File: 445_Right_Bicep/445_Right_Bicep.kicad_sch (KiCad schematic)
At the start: 7 parts, among them J1 69167-114HLF, J2 SM02B-SRSS-TB_LF__SN_, J3 87583-2010RPLF, U1 ESP32-S3-WROOM-1-N16R8, U2 LSM6DSMTR, U3 LP2950CZ-3.3_LFT3

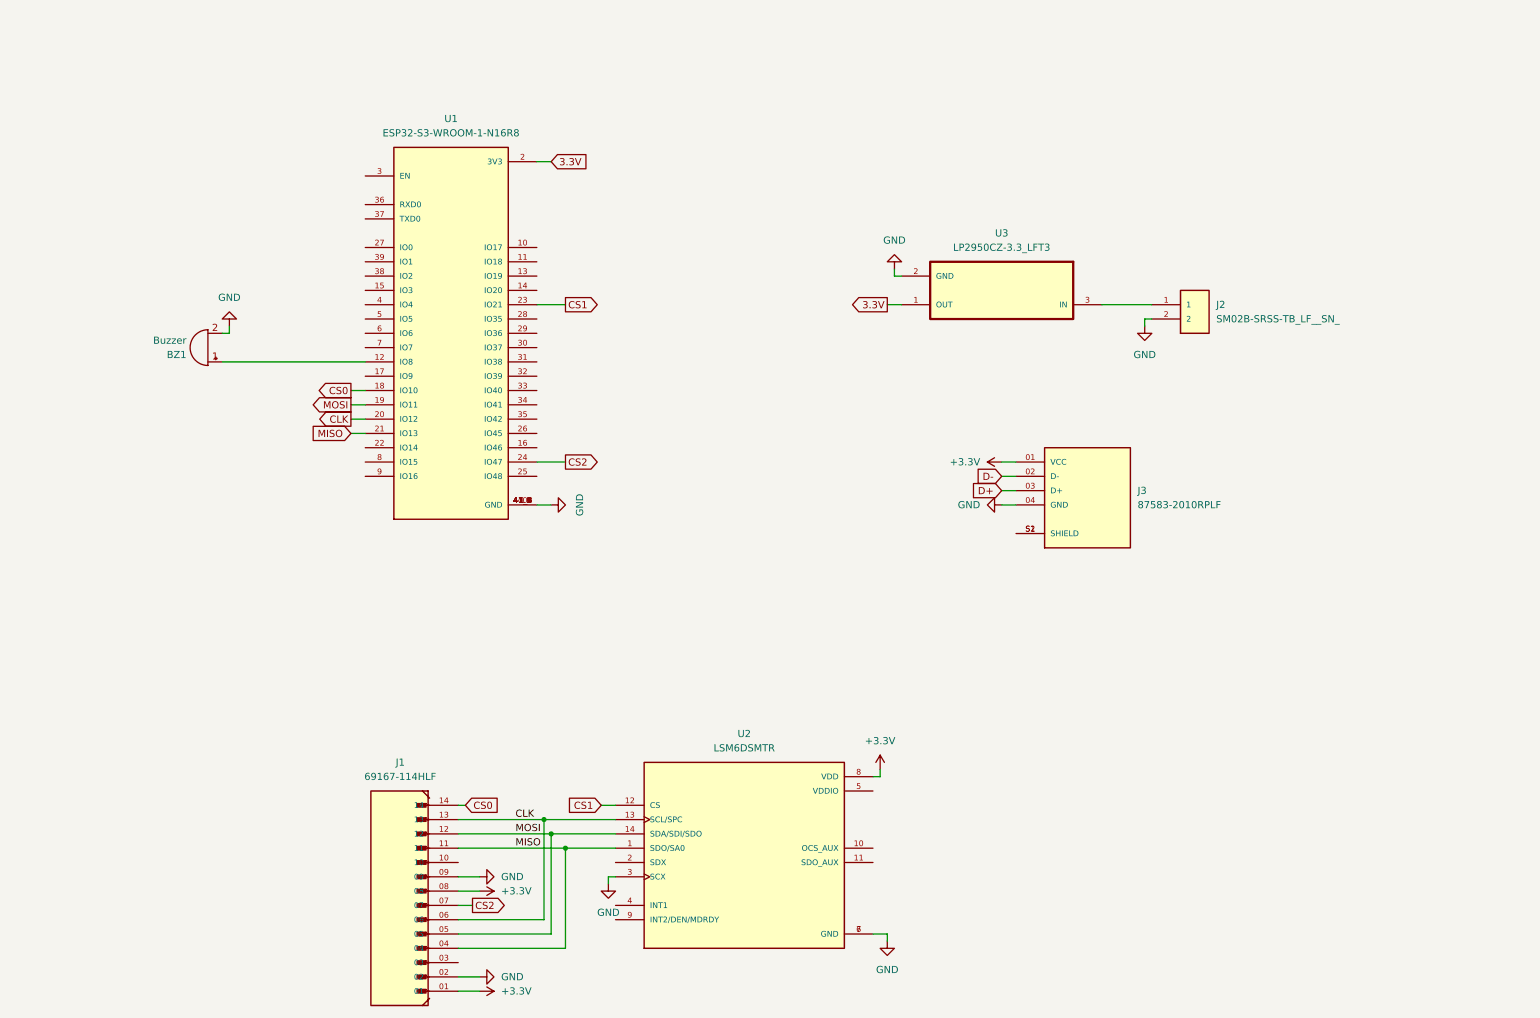
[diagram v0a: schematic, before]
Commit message: enable signal and analog switches
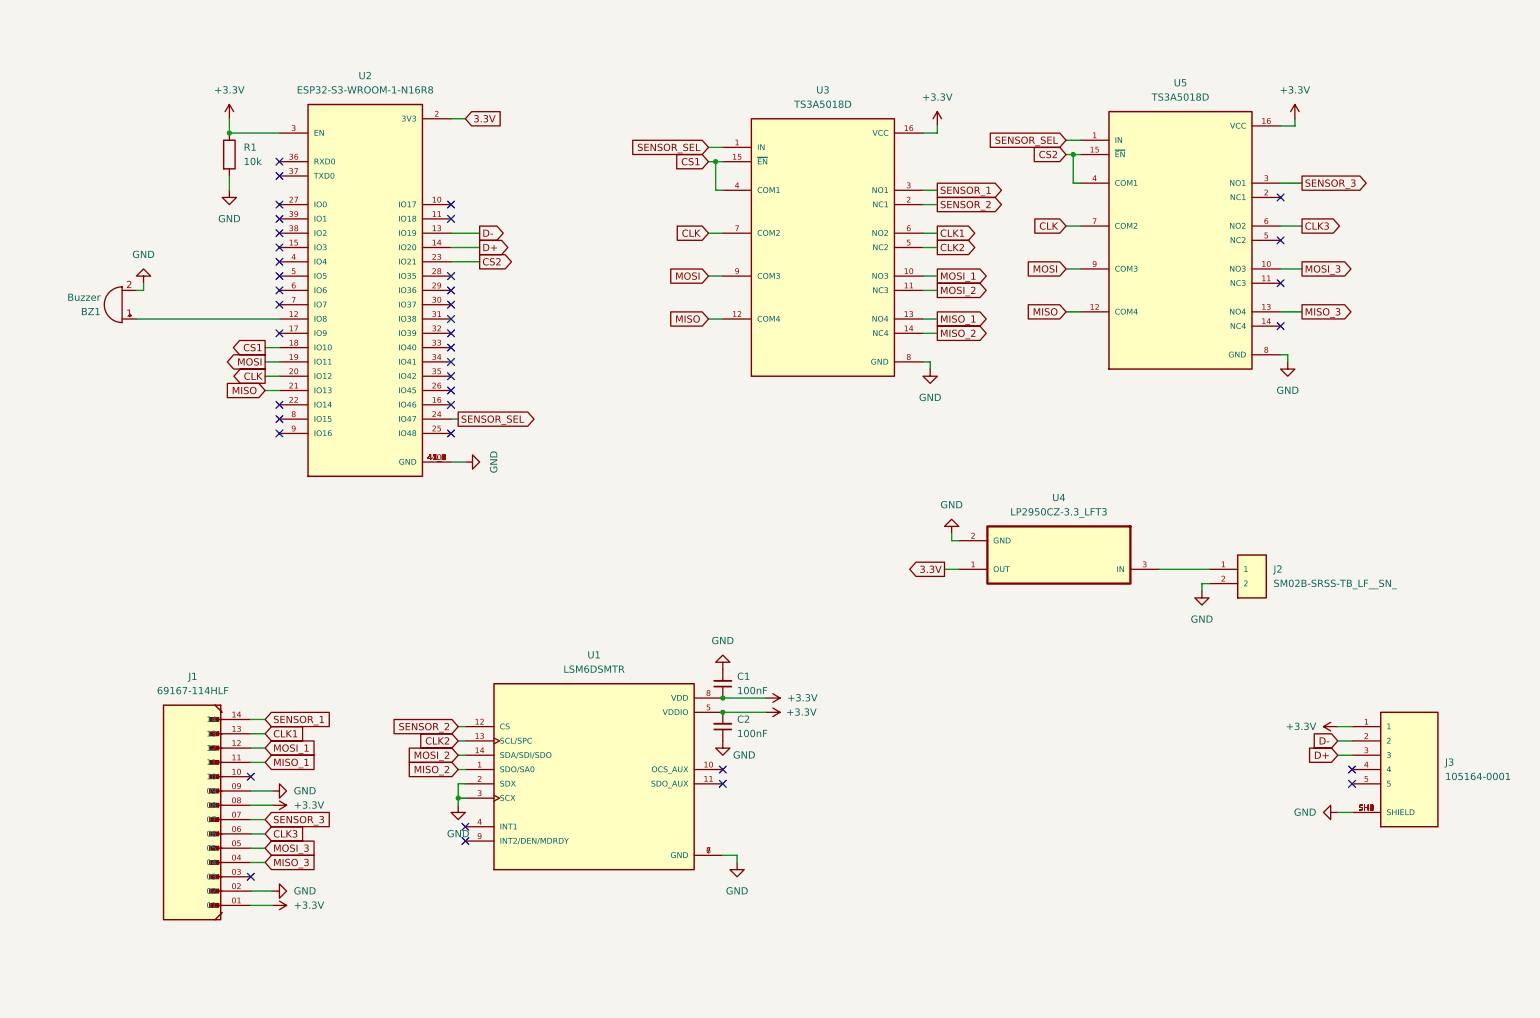
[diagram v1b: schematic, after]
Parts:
- removed J3: 87583-2010RPLF, 87583-2010RPLF:AMPHENOL_87583-2010RPLF, symbol 87583-2010RPLF:87583-2010RPLF
- removed U1: ESP32-S3-WROOM-1-N16R8, ESP32-S3-WROOM-1-N16R8:XCVR_ESP32-S3-WROOM-1-N16R8, symbol ESP32-S3-WROOM-1-N16R8:ESP32-S3-WROOM-1-N16R8
- removed U2: LSM6DSMTR, LSM6DSMTR (1):PQFN50P300X250X86-14N, symbol LSM6DSMTR:LSM6DSMTR
- removed U3: LP2950CZ-3.3_LFT3, LP2950CZ-3.3_LFT3:TO92127P521H735-3, symbol LP2950CZ-3.3_LFT3:LP2950CZ-3.3_LFT3
- added C1, C2: 100nF, symbol Device:C_Small
- added J3: 105164-0001, 105164-0001:MOLEX_105164-0001, symbol 105164-0001:105164-0001
- added R1: 10k, symbol Device:R
- added U1: LSM6DSMTR, LSM6DSMTR (1):PQFN50P300X250X86-14N, symbol LSM6DSMTR:LSM6DSMTR
- added U2: ESP32-S3-WROOM-1-N16R8, ESP32-S3-WROOM-1-N16R8:XCVR_ESP32-S3-WROOM-1-N16R8, symbol ESP32-S3-WROOM-1-N16R8:ESP32-S3-WROOM-1-N16R8
- added U3, U5: TS3A5018D, TS3A5018D:SOIC127P600X175-16N, symbol TS3A5018D:TS3A5018D
- added U4: LP2950CZ-3.3_LFT3, LP2950CZ-3.3_LFT3:TO92127P521H735-3, symbol LP2950CZ-3.3_LFT3:LP2950CZ-3.3_LFT3
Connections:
- net +3.3V: now also C1.1, C2.2, J3.1, R1.1, U1.5 (VDDIO), U1.8 (VDD), U2.3 (EN), U3.16 (VCC), U5.16 (VCC)
- net 3.3V: now also U2.2 (3V3), U4.1 (OUT)
- net CLK: now also U2.20 (IO12), U3.7 (COM2), U5.7 (COM2); no longer J1.06, J1.13
- net CS1: now also U2.18 (IO10), U3.15 (~{EN}), U3.4 (COM1)
- net CS2: now also U2.23 (IO21), U5.15 (~{EN}), U5.4 (COM1); no longer J1.07
- net D+: now also J3.3, U2.14 (IO20)
- net D-: now also J3.2, U2.13 (IO19)
- net GND: now also C1.2, C2.1, J3.SH1 (SHIELD), J3.SH2 (SHIELD), J3.SH3 (SHIELD), J3.SH4 (SHIELD), J3.SH5 (SHIELD), J3.SH6 (SHIELD), R1.2, U1.2 (SDX), U1.3 (SCX), U1.6 (GND), U1.7 (GND), U2.1 (GND), U2.40 (GND), U2.41_1 (GND), U2.41_2 (GND), U2.41_3 (GND), U2.41_4 (GND), U2.41_5 (GND), U2.41_6 (GND), U2.41_7 (GND), U2.41_8 (GND), U2.41_9 (GND), U3.8 (GND), U4.2 (GND), U5.8 (GND)
- net MISO: now also U2.21 (IO13), U3.12 (COM4), U5.12 (COM4); no longer J1.04, J1.11
- net MOSI: now also U2.19 (IO11), U3.9 (COM3), U5.9 (COM3); no longer J1.05, J1.12
- net at BZ1.1 (+): now also U2.12 (IO8)
- net at J2.1: now also U4.3 (IN)
- net CS0 renamed SENSOR_1
- net SENSOR_1: now also U3.3 (NO1)
- new net CLK1: J1.13, U3.6 (NO2)
- new net CLK2: U1.13 (SCL/SPC), U3.5 (NC2)
- new net CLK3: J1.06, U5.6 (NO2)
- new net MISO_1: J1.11, U3.13 (NO4)
- new net MISO_2: U1.1 (SDO/SA0), U3.14 (NC4)
- new net MISO_3: J1.04, U5.13 (NO4)
- new net MOSI_1: J1.12, U3.10 (NO3)
- new net MOSI_2: U1.14 (SDA/SDI/SDO), U3.11 (NC3)
- new net MOSI_3: J1.05, U5.10 (NO3)
- new net SENSOR_2: U1.12 (CS), U3.2 (NC1)
- new net SENSOR_3: J1.07, U5.3 (NO1)
- new net SENSOR_SEL: U2.24 (IO47), U3.1 (IN), U5.1 (IN)
- no-connect marks 0 -> 39

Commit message: replace bicep connector and add int1 connections
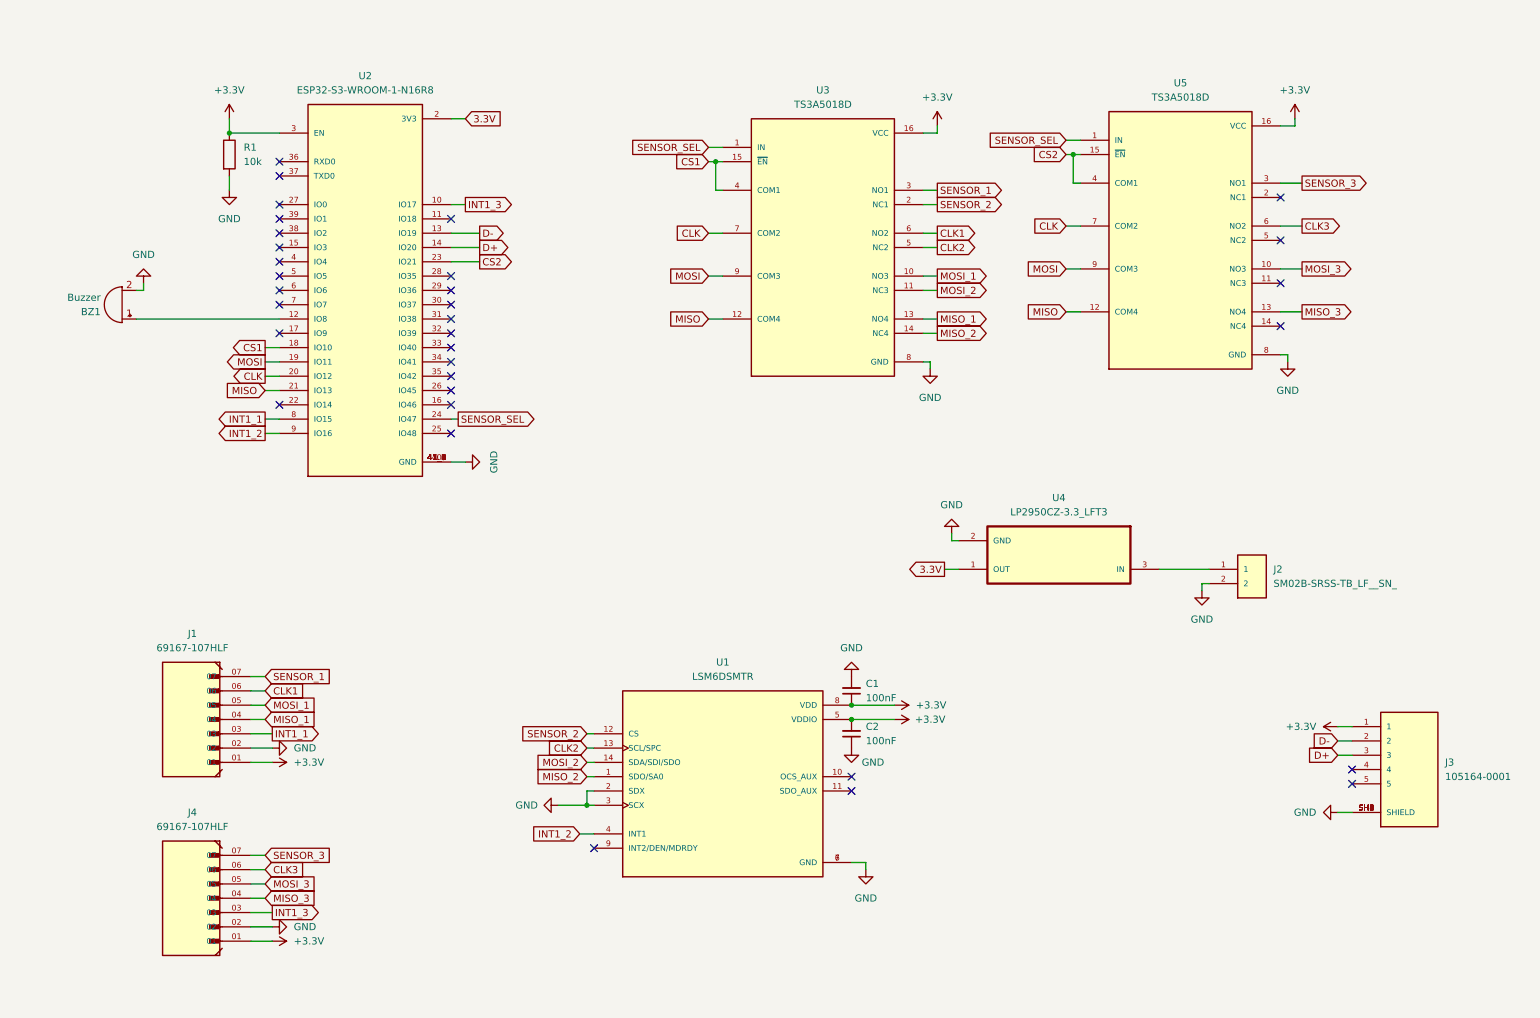
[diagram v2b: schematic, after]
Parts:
- removed J1: 69167-114HLF, 69167-114HLF:AMPHENOL_69167-114HLF, symbol 69167-114HLF:69167-114HLF
- added J1, J4: 69167-107HLF, 69167-107HLF:AMPHENOL_69167-107HLF, symbol 69167-107HLF:69167-107HLF
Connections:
- net +3.3V: now also J1.01, J4.01
- net CLK1: now also J1.06
- net CLK3: now also J4.06
- net GND: now also J1.02, J4.02
- net MISO_1: now also J1.04
- net MISO_3: now also J4.04
- net MOSI_1: now also J1.05
- net MOSI_3: now also J4.05
- net SENSOR_1: now also J1.07
- net SENSOR_3: now also J4.07
- net INT1_3: now reaches U2.10 (IO17)
- net INT1_3: now also J4.03
- net INT1_1: now reaches U2.8 (IO15)
- net INT1_1: now also J1.03
- net INT1_2: now reaches U2.9 (IO16)
- net INT1_2: now also U1.4 (INT1)
- no-connect marks 39 -> 33
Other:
- moved on the sheet: C1, C2, U1

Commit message: Layout First Draft
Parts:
- removed J3: 105164-0001, 105164-0001:MOLEX_105164-0001, symbol 105164-0001:105164-0001
- added H1, H2, H3, H4: MountingHole, MountingHole:MountingHole_2mm, symbol Mechanical:MountingHole
- added J10: 87583-2010RPLF, 87583-2010RPLF:AMPHENOL_87583-2010RPLF, symbol 87583-2010RPLF:87583-2010RPLF
- renumbered C1 to C11, C2 to C12, J4 to J12, J1 to J5, J2 to J8, R1 to R2, U4 to U10, U3 to U13, U5 to U14, U1 to U7
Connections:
- net 3.3V is gone; now on net +3.3V: U10.1 (OUT), U2.2 (3V3)
- net +3.3V: now also J10.01 (VCC)
- net D+: now also J10.03 (D+)
- net D-: now also J10.02 (D-)
- net GND: now also J10.04 (GND)
- net MISO: now also U2.19 (IO11); no longer U2.21 (IO13)
- net MOSI: now also U2.21 (IO13); no longer U2.19 (IO11)
- new net: J10.S1 (SHIELD), J10.S2 (SHIELD)
- no-connect marks 33 -> 32

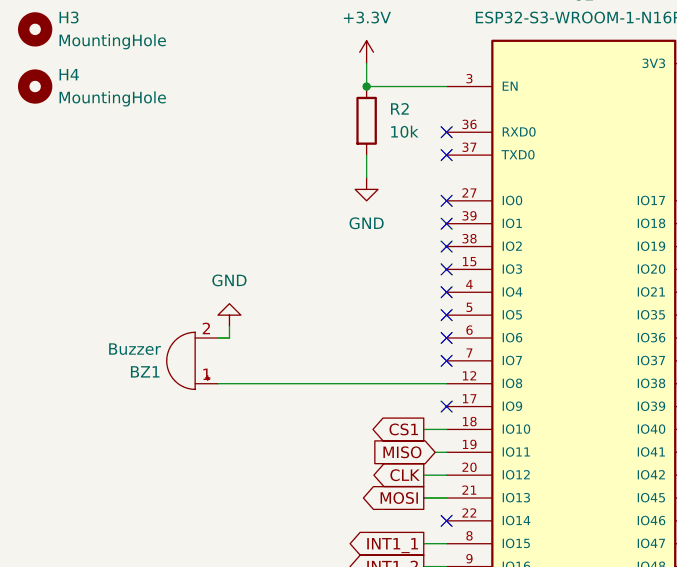
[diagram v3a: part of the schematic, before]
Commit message: adding buzzer
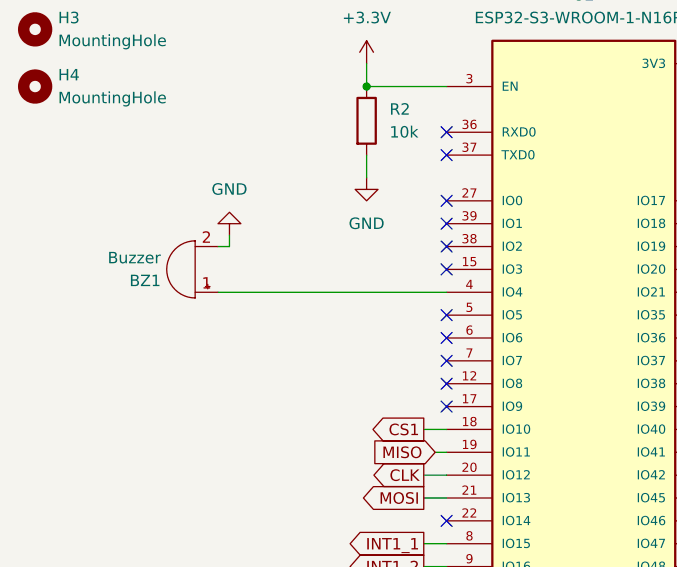
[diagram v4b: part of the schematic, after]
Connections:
- net at BZ1.1 (+): now also U2.4 (IO4); no longer U2.12 (IO8)
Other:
- moved on the sheet: BZ1
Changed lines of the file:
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@@
   (no_connect (at 62.23 49.53))
   (no_connect (at 92.71 85.09))
-  (no_connect (at 62.23 59.69))
   (no_connect (at 92.71 80.01))
   (no_connect (at 92.71 52.07))
@@
   (no_connect (at 92.71 82.55))
   (no_connect (at 62.23 62.23))
+  (no_connect (at 62.23 69.85))
   (no_connect (at 240.03 55.88))
   (no_connect (at 62.23 72.39))
@@
     (stroke (width 0) (type default))
   )
+  (wire (pts (xy 36.83 59.69) (xy 62.23 59.69))
+    (stroke (width 0) (type default))
+  )
   (wire (pts (xy 116.84 151.13) (xy 118.11 151.13))
     (stroke (width 0) (type default))
@@
     (stroke (width 0) (type default))
   )
-  (wire (pts (xy 38.1 63.5) (xy 38.1 64.77))
+  (wire (pts (xy 38.1 53.34) (xy 38.1 54.61))
     (stroke (width 0) (type default))
   )
@@
     (stroke (width 0) (type default))
   )
-  (wire (pts (xy 36.83 69.85) (xy 62.23 69.85))
-    (stroke (width 0) (type default))
-  )
   (wire (pts (xy 60.96 77.47) (xy 62.23 77.47))
     (stroke (width 0) (type default))
@@
     (stroke (width 0) (type default))
   )
-  (wire (pts (xy 38.1 64.77) (xy 36.83 64.77))
+  (wire (pts (xy 38.1 54.61) (xy 36.83 54.61))
     (stroke (width 0) (type default))
   )
@@
     )
   )
-  (symbol (lib_id "Device:Buzzer") (at 34.29 67.31 180) (unit 1)
-    (in_bom yes) (on_board yes) (dnp no) (fields_autoplaced)
-    (property "Reference" "BZ1" (at 30.48 68.58 0)
+  (symbol (lib_id "Device:Buzzer") (at 34.29 57.15 180) (unit 1)
+    (in_bom yes) (on_board yes) (dnp no) (fields_autoplaced)
+    (property "Reference" "BZ1" (at 30.48 58.42 0)
       (effects (font (size 1.27 1.27)) (justify left))
     )
-    (property "Value" "Buzzer" (at 30.48 66.04 0)
+    (property "Value" "Buzzer" (at 30.48 55.88 0)
       (effects (font (size 1.27 1.27)) (justify left))
     )
-    (property "Footprint" "ECE 445 Footprints:AC-903-D-1P" (at 34.925 69.85 90)
-      (effects (font (size 1.27 1.27)) hide)
-    )
-    (property "Datasheet" "~" (at 34.925 69.85 90)
+    (property "Footprint" "ECE 445 Footprints:AC-903-D-1P" (at 34.925 59.69 90)
+      (effects (font (size 1.27 1.27)) hide)
+    )
+    (property "Datasheet" "~" (at 34.925 59.69 90)
       (effects (font (size 1.27 1.27)) hide)
     )
@@
     )
   )
-  (symbol (lib_id "power:GND") (at 38.1 63.5 180) (unit 1)
-    (in_bom yes) (on_board yes) (dnp no) (fields_autoplaced)
-    (property "Reference" "#PWR06" (at 38.1 57.15 0)
-      (effects (font (size 1.27 1.27)) hide)
-    )
-    (property "Value" "GND" (at 38.1 58.42 0)
+  (symbol (lib_id "power:GND") (at 38.1 53.34 180) (unit 1)
+    (in_bom yes) (on_board yes) (dnp no) (fields_autoplaced)
+    (property "Reference" "#PWR06" (at 38.1 46.99 0)
+      (effects (font (size 1.27 1.27)) hide)
+    )
+    (property "Value" "GND" (at 38.1 48.26 0)
       (effects (font (size 1.27 1.27)))
     )
-    (property "Footprint" "" (at 38.1 63.5 0)
-      (effects (font (size 1.27 1.27)) hide)
-    )
-    (property "Datasheet" "" (at 38.1 63.5 0)
-      (effects (font (size 1.27 1.27)) hide)
-    )
+    (property "Footprint" "" (at 38.1 53.34 0)
+      (effects (font (size 1.27 1.27)) hide)
+    )
+    (property "Datasheet" "" (at 38.1 53.34 0)
+      (effects (font (size 1.27 1.27)) hide)
+    )

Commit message: D+ and D- as differential pairs
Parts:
- C11, C12: footprint (none) -> CL21F104ZAANNNC:CAPC2012X135N
- R2: footprint (none) -> RMCF0805JG10K0:RESC2012X65N
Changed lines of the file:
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@@
       (effects (font (size 1.27 1.27)) (justify right))
     )
-    (property "Footprint" "" (at 163.83 135.89 0)
+    (property "Footprint" "CL21F104ZAANNNC:CAPC2012X135N" (at 163.83 135.89 0)
       (effects (font (size 1.27 1.27)) hide)
     )
@@
       (effects (font (size 1.27 1.27)) (justify right))
     )
-    (property "Footprint" "" (at 163.83 143.51 0)
+    (property "Footprint" "CL21F104ZAANNNC:CAPC2012X135N" (at 163.83 143.51 0)
       (effects (font (size 1.27 1.27)) hide)
     )
@@
       (effects (font (size 1.27 1.27)) (justify left))
     )
-    (property "Footprint" "" (at 51.562 40.64 90)
-      (effects (font (size 1.27 1.27)) hide)
-    )
+    (property "Footprint" "RMCF0805JG10K0:RESC2012X65N" (at 51.562 40.64 90)
+      (effects (font (size 1.27 1.27)) hide)
+    )
